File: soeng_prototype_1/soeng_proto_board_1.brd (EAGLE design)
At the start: 86.3 x 37.8 mm, 11 parts, among them J1 2172034-1

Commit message: PCB Rev. 2
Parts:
- removed CN1: (no value), adafruit:JST-PH-2-THM-RA
- added R1: 10, adafruit:0207/9
- added SPKR+, SPKR-: WIREPAD1,6/0,8, wirepad:1,6/0,8
- added T1: 2N2222, adafruit:TO92-EBC-OVAL
- moved C3 8.89 mm to (53.3, 30.5), turned to 180 degrees
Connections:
- new net N$9: R1.1, SPKR+.1
- net +5V: now also T1.C
- net GND: now also SPKR-.1
- net N$4: now also T1.B; no longer CN1.1
- net N$6: now also R1.2, T1.E; no longer CN1.2, U$1.1.5
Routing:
- net +5V: track 65.8 -> 81.1 mm
- net N$9: track 0.00 -> 10.8 mm
- net N$6: track 10.0 -> 6.11 mm
- net N$5: track 27.7 -> 30.9 mm
- net N$3: track 56.5 -> 59.6 mm, vias 0 -> 1
- net N$2: track 57.5 -> 55.9 mm
- net N$1: track 56.0 -> 57.1 mm
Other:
- board text added: "5V"
- board text added: "DIN"
- board text added: "Insert pushbuttons from other side, and match alignment of flats"
- board text added: "This end mates w/ TOP of 5-pin conn on right side of dot matrix displ"
- board text added: "VCC"
- board text removed: "+5V"

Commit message: Rev. 3
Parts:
- removed SPKR+, SPKR-: WIREPAD1,6/0,8, wirepad:1,6/0,8
- added U$4: MICRO_SPKR, lap_2019:MICRO_SPKR
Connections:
- net GND: now also U$4.P$2; no longer SPKR-.1
- net N$9: now also U$4.P$1; no longer SPKR+.1
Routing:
- net N$9: track 10.8 -> 9.49 mm
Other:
- board text added: "ALIGN FLATS IN PUSHBUTTONS WITH OUTLINE!!"
- board text added: "Engineering"
- board text added: "Insert pushbuttons from other side"
- board text added: "PN2222A"
- board text added: "SPKR+"
- board text added: "SPKR-"
- board text added: "TCNJ"
- board text removed: "Insert pushbuttons from other side, and match alignment of flats"
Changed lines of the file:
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@@
 <?xml version="1.0" encoding="utf-8"?>
 <!DOCTYPE eagle SYSTEM "eagle.dtd">
-<eagle version="9.5.2">
+<eagle version="9.6.2">
 <drawing>
 <settings>
@@
 <wire x1="29.718" y1="11.938" x2="29.718" y2="3.048" width="0.1524" layer="26" grouprefs="PUSHBUTTON1"/>
 <wire x1="29.718" y1="11.938" x2="29.718" y2="3.048" width="0.1524" layer="26" curve="-270" grouprefs="PUSHBUTTON1"/>
-<wire x1="11.43" y1="11.684" x2="11.43" y2="2.794" width="0.1524" layer="25" curve="-270"/>
-<wire x1="11.43" y1="11.684" x2="11.43" y2="2.794" width="0.1524" layer="25"/>
-<wire x1="29.464" y1="11.684" x2="29.464" y2="2.794" width="0.1524" layer="25"/>
-<wire x1="29.464" y1="11.684" x2="29.464" y2="2.794" width="0.1524" layer="25" curve="-270"/>
-<text x="19.05" y="11.43" size="1.016" layer="25">Insert pushbuttons from
-other side, and match
-alignment of flats</text>
+<text x="11.684" y="7.112" size="1.27" layer="25">Insert pushbuttons from other side</text>
+<text x="82.042" y="27.686" size="0.8128" layer="25">SPKR+</text>
+<text x="82.042" y="21.336" size="0.8128" layer="25">SPKR-</text>
+<text x="48.26" y="34.29" size="0.8128" layer="25">PN2222A</text>
+<text x="25.4" y="15.24" size="1.27" layer="26" rot="MR0" align="center">ALIGN FLATS IN PUSHBUTTONS
+WITH OUTLINE!!</text>
+<circle x="51.816" y="23.368" radius="0.254" width="0.1524" layer="22"/>
+<circle x="54.356" y="23.368" radius="0.254" width="0.1524" layer="22"/>
+<circle x="56.896" y="23.368" radius="0.254" width="0.1524" layer="22"/>
+<circle x="59.436" y="23.368" radius="0.254" width="0.1524" layer="22"/>
+<circle x="61.976" y="23.368" radius="0.254" width="0.1524" layer="22"/>
+<circle x="69.596" y="23.368" radius="0.254" width="0.1524" layer="22"/>
+<circle x="72.136" y="23.368" radius="0.254" width="0.1524" layer="22"/>
+<circle x="74.676" y="23.368" radius="0.254" width="0.1524" layer="22"/>
+<circle x="43.18" y="19.05" radius="0.254" width="0.1524" layer="22"/>
+<circle x="43.18" y="16.51" radius="0.254" width="0.1524" layer="22"/>
+<circle x="80.264" y="26.67" radius="0.254" width="0.1524" layer="22"/>
+<circle x="80.264" y="22.86" radius="0.254" width="0.1524" layer="22"/>
+<circle x="54.61" y="36.322" radius="0.254" width="0.1524" layer="22"/>
+<circle x="57.15" y="36.322" radius="0.254" width="0.1524" layer="22"/>
+<circle x="59.69" y="36.322" radius="0.254" width="0.1524" layer="22"/>
+<circle x="43.18" y="36.576" radius="0.254" width="0.1524" layer="22"/>
+<circle x="40.64" y="36.576" radius="0.254" width="0.1524" layer="22"/>
+<circle x="38.1" y="36.576" radius="0.254" width="0.1524" layer="22"/>
+<circle x="24.13" y="36.576" radius="0.254" width="0.1524" layer="22"/>
+<circle x="21.59" y="36.576" radius="0.254" width="0.1524" layer="22"/>
+<circle x="19.05" y="36.576" radius="0.254" width="0.1524" layer="22"/>
+<circle x="16.51" y="36.576" radius="0.254" width="0.1524" layer="22"/>
+<circle x="13.97" y="36.576" radius="0.254" width="0.1524" layer="22"/>
+<circle x="6.858" y="22.86" radius="0.254" width="0.1524" layer="22"/>
+<circle x="6.858" y="17.272" radius="0.254" width="0.1524" layer="22"/>
+<circle x="3.81" y="16.256" radius="0.254" width="0.1524" layer="22"/>
+<circle x="3.81" y="23.876" radius="0.254" width="0.1524" layer="22"/>
+<circle x="65.278" y="34.544" radius="0.254" width="0.1524" layer="21"/>
+<circle x="65.278" y="34.544" radius="0.254" width="0.1524" layer="22"/>
+<circle x="74.422" y="34.544" radius="0.254" width="0.1524" layer="22"/>
+<text x="63.5" y="17.78" size="6.4516" layer="22" rot="MR0" align="center">TCNJ</text>
+<text x="63.5" y="11.43" size="3.175" layer="22" rot="MR0" align="center">Engineering</text>
 </plain>
 <attributes>
@@
 <attribute name="VALUE" x="59.69" y="37.592" size="1.27" layer="27" ratio="10" rot="R180"/>
 </element>
-<element name="SPKR+" library="wirepad" library_urn="urn:adsk.eagle:library:412" package="1,6/0,8" package3d_urn="urn:adsk.eagle:package:30830/1" value="WIREPAD1,6/0,8" x="82.55" y="26.67" smashed="yes">
-<attribute name="NAME" x="79.248" y="27.686" size="1.27" layer="25" ratio="10"/>
-<attribute name="POPULARITY" value="1" x="82.55" y="26.67" size="1.778" layer="27" display="off"/>
-<attribute name="VALUE" x="82.55" y="27.27" size="0.0254" layer="27"/>
-</element>
-<element name="SPKR-" library="wirepad" library_urn="urn:adsk.eagle:library:412" package="1,6/0,8" package3d_urn="urn:adsk.eagle:package:30830/1" value="WIREPAD1,6/0,8" x="82.55" y="22.86" smashed="yes">
-<attribute name="NAME" x="79.248" y="23.876" size="1.27" layer="25" ratio="10"/>
-<attribute name="POPULARITY" value="1" x="82.55" y="22.86" size="1.778" layer="27" display="off"/>
-<attribute name="VALUE" x="82.55" y="23.46" size="0.0254" layer="27"/>
-</element>
 <element name="R1" library="adafruit" library_urn="urn:adsk.eagle:library:420" package="0207/9" package3d_urn="urn:adsk.eagle:package:6240935/1" value="10" x="69.85" y="33.02" smashed="yes" rot="R180">
 <attribute name="NAME" x="72.898" y="31.496" size="1.27" layer="25" ratio="10" rot="R180"/>
 <attribute name="VALUE" x="72.1106" y="33.655" size="1.27" layer="27" ratio="10" rot="R180"/>
 </element>
+<element name="U$4" library="lap_2019" package="MICRO_SPKR" value="MICRO_SPKR" x="81.28" y="26.67" smashed="yes" rot="R270"/>
 </elements>
 <signals>
@@
 <contactref element="C1" pad="2"/>
 <contactref element="DOT_MATRIX_DISPLAY" pad="2"/>
-<contactref element="SPKR-" pad="1"/>
+<contactref element="U$4" pad="P$2"/>
 </signal>
 <signal name="+5V">
@@
 <signal name="N$9">
 <contactref element="R1" pad="1"/>
-<contactref element="SPKR+" pad="1"/>
-<wire x1="80.772" y1="26.67" x2="82.55" y2="26.67" width="0.1524" layer="1"/>
+<contactref element="U$4" pad="P$1"/>
+<wire x1="80.772" y1="26.67" x2="81.28" y2="26.67" width="0.1524" layer="1"/>
 <wire x1="74.422" y1="33.02" x2="80.772" y2="26.67" width="0.1524" layer="1"/>
 </signal>

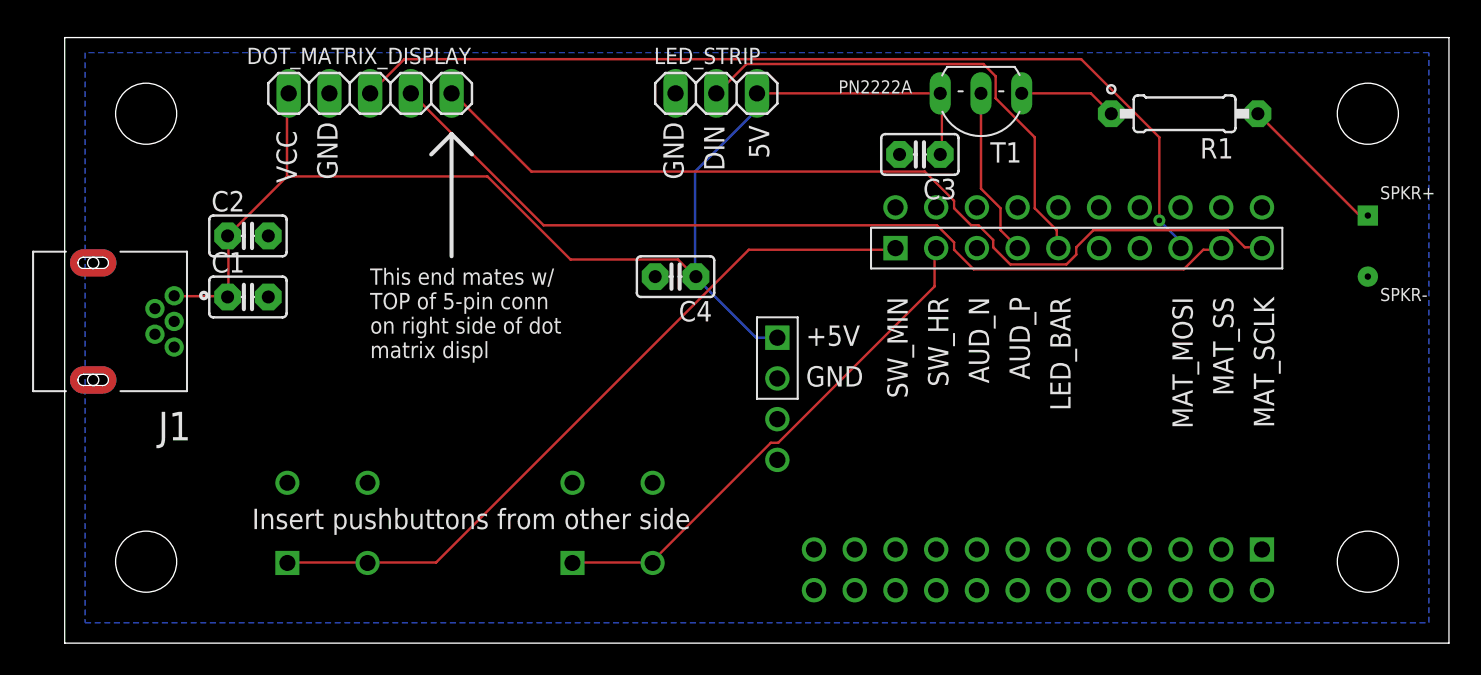
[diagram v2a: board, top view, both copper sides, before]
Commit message: Added TCXO, 3.3V Zener, RC
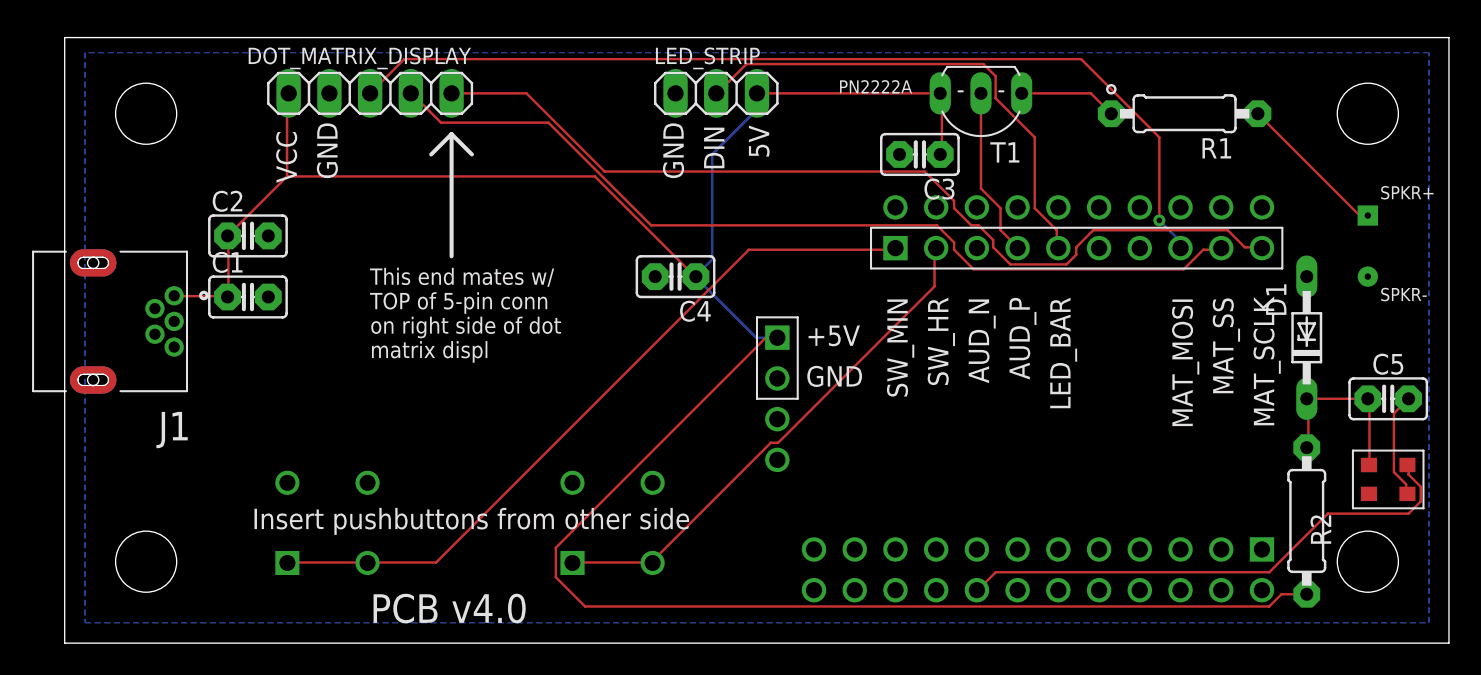
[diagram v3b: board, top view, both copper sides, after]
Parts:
- added C5: (no value), adafruit:C025-025X050
- added D1: (no value), diode:DO34Z7
- added R2: 10, adafruit:0207/9
- added U$5: TXEAPLSANF, lap_2019:TXEAPLSANF
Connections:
- new net N$10: U$1.2.7, U$5.TCXO3
- new net N$11: C5.1, D1.C, R2.1, U$5.TCXO4
- net +5V: now also R2.2
- net GND: now also C5.2, D1.A, U$5.TCXO2
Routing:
- net +5V: track 81.1 -> 150.1 mm
- net N$10: track 0.00 -> 32.6 mm
- net N$11: track 0.00 -> 11.2 mm
- net GND: track 0.00 -> 6.65 mm
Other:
- board text added: "Larry Pearlstein, Elli Lopez"
- board text added: "PCB v4.0"
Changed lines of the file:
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@@
 <text x="63.5" y="17.78" size="6.4516" layer="22" rot="MR0" align="center">TCNJ</text>
 <text x="63.5" y="11.43" size="3.175" layer="22" rot="MR0" align="center">Engineering</text>
+<text x="74.93" y="7.62" size="0.762" layer="22" rot="MR0">Larry Pearlstein, Elli Lopez</text>
+<text x="19.05" y="1.27" size="1.778" layer="25">PCB v4.0</text>
 </plain>
 <attributes>
@@
 </element>
 <element name="U$4" library="lap_2019" package="MICRO_SPKR" value="MICRO_SPKR" x="81.28" y="26.67" smashed="yes" rot="R270"/>
+<element name="U$5" library="lap_2019" package="TXEAPLSANF" value="TXEAPLSANF" x="82.55" y="10.16" smashed="yes"/>
+<element name="D1" library="diode" library_urn="urn:adsk.eagle:library:210" package="DO34Z7" package3d_urn="urn:adsk.eagle:package:43364/1" value="" x="77.47" y="19.05" smashed="yes" rot="R90">
+<attribute name="NAME" x="76.2" y="20.32" size="1.27" layer="25" ratio="10" rot="R90"/>
+<attribute name="POPULARITY" value="3" x="77.47" y="19.05" size="1.778" layer="27" rot="R90" display="off"/>
+<attribute name="VALUE" x="79.883" y="17.526" size="1.27" layer="27" ratio="10" rot="R90"/>
+</element>
+<element name="R2" library="adafruit" library_urn="urn:adsk.eagle:library:420" package="0207/9" package3d_urn="urn:adsk.eagle:package:6240935/1" value="10" x="77.47" y="7.62" smashed="yes" rot="R270">
+<attribute name="NAME" x="77.724" y="8.128" size="1.27" layer="25" ratio="10" rot="R270"/>
+<attribute name="VALUE" x="76.835" y="9.8806" size="1.27" layer="27" ratio="10" rot="R270"/>
+</element>
+<element name="C5" library="adafruit" library_urn="urn:adsk.eagle:library:420" package="C025-025X050" package3d_urn="urn:adsk.eagle:package:6240323/1" value="" x="82.55" y="15.24" smashed="yes">
+<attribute name="NAME" x="81.534" y="16.764" size="1.27" layer="25" ratio="10"/>
+<attribute name="VALUE" x="80.264" y="12.446" size="1.27" layer="27" ratio="10"/>
+</element>
 </elements>
 <signals>
@@
 <wire x1="55.4736" y1="27.5844" x2="55.4736" y2="27.1272" width="0.1524" layer="1"/>
 <wire x1="53.6448" y1="29.4132" x2="55.4736" y2="27.5844" width="0.1524" layer="1"/>
-<wire x1="29.1084" y1="29.4132" x2="53.6448" y2="29.4132" width="0.1524" layer="1"/>
-<wire x1="24.2316" y1="34.29" x2="29.1084" y2="29.4132" width="0.1524" layer="1"/>
+<wire x1="33.6804" y1="29.4132" x2="53.6448" y2="29.4132" width="0.1524" layer="1"/>
+<wire x1="28.8036" y1="34.29" x2="33.6804" y2="29.4132" width="0.1524" layer="1"/>
+<wire x1="24.13" y1="34.29" x2="28.8036" y2="34.29" width="0.1524" layer="1"/>
 <wire x1="74.676" y1="24.6888" x2="74.676" y2="24.638" width="0.1524" layer="1"/>
-<wire x1="24.2316" y1="34.29" x2="24.13" y2="34.29" width="0.1524" layer="1"/>
 </signal>
 <signal name="N$2">
@@
 <wire x1="55.4736" y1="24.9936" x2="55.4736" y2="24.5364" width="0.1524" layer="1"/>
 <wire x1="54.4068" y1="26.0604" x2="55.4736" y2="24.9936" width="0.1524" layer="1"/>
-<wire x1="29.8704" y1="26.0604" x2="54.4068" y2="26.0604" width="0.1524" layer="1"/>
-<wire x1="21.6408" y1="34.29" x2="29.8704" y2="26.0604" width="0.1524" layer="1"/>
+<wire x1="36.576" y1="26.0604" x2="54.4068" y2="26.0604" width="0.1524" layer="1"/>
+<wire x1="30.1752" y1="32.4612" x2="36.576" y2="26.0604" width="0.1524" layer="1"/>
+<wire x1="23.4696" y1="32.4612" x2="30.1752" y2="32.4612" width="0.1524" layer="1"/>
+<wire x1="21.6408" y1="34.29" x2="23.4696" y2="32.4612" width="0.1524" layer="1"/>
 <wire x1="72.0852" y1="24.5364" x2="72.136" y2="24.638" width="0.1524" layer="1"/>
 <wire x1="21.6408" y1="34.29" x2="21.59" y2="34.29" width="0.1524" layer="1"/>
@@
 <contactref element="DOT_MATRIX_DISPLAY" pad="2"/>
 <contactref element="U$4" pad="P$2"/>
+<contactref element="U$5" pad="TCXO2"/>
+<contactref element="D1" pad="A"/>
+<contactref element="C5" pad="2"/>
+<wire x1="83.6676" y1="9.906" x2="83.6676" y2="9.4488" width="0.1524" layer="1"/>
+<wire x1="82.9056" y1="10.668" x2="83.6676" y2="9.906" width="0.1524" layer="1"/>
+<wire x1="82.9056" y1="14.3256" x2="82.9056" y2="10.668" width="0.1524" layer="1"/>
+<wire x1="83.82" y1="15.24" x2="82.9056" y2="14.3256" width="0.1524" layer="1"/>
+<wire x1="83.6676" y1="9.4488" x2="83.75" y2="9.31" width="0.1524" layer="1"/>
 </signal>
 <signal name="+5V">
@@
 <contactref element="DOT_MATRIX_DISPLAY" pad="1"/>
 <contactref element="T1" pad="C"/>
+<contactref element="R2" pad="2"/>
 <wire x1="10.0584" y1="21.6408" x2="6.858" y2="21.6408" width="0.1524" layer="1"/>
 <wire x1="6.858" y1="21.6408" x2="6.828" y2="21.666" width="0.1524" layer="1"/>
@@
 <wire x1="10.2108" y1="21.6408" x2="10.16" y2="21.59" width="0.1524" layer="1"/>
 <wire x1="10.2108" y1="25.2984" x2="10.16" y2="25.4" width="0.1524" layer="1"/>
-<wire x1="43.1292" y1="19.05" x2="44.45" y2="19.05" width="0.1524" layer="16"/>
-<wire x1="39.3192" y1="22.86" x2="43.1292" y2="19.05" width="0.1524" layer="16"/>
 <wire x1="54.7116" y1="30.48" x2="54.7116" y2="34.29" width="0.1524" layer="1"/>
 <wire x1="54.7116" y1="34.29" x2="54.61" y2="34.29" width="0.1524" layer="1"/>
 <wire x1="54.7116" y1="30.48" x2="54.61" y2="30.48" width="0.1524" layer="1"/>
 <wire x1="54.61" y1="34.29" x2="43.18" y2="34.29" width="0.1524" layer="1"/>
-<wire x1="39.3192" y1="29.4132" x2="39.3192" y2="22.86" width="0.1524" layer="16"/>
-<wire x1="43.1292" y1="33.2232" x2="39.3192" y2="29.4132" width="0.1524" layer="16"/>
-<wire x1="43.1292" y1="34.29" x2="43.1292" y2="33.2232" width="0.1524" layer="16"/>
+<wire x1="43.1292" y1="19.05" x2="44.45" y2="19.05" width="0.1524" layer="16"/>
+<wire x1="39.3192" y1="22.86" x2="43.1292" y2="19.05" width="0.1524" layer="16"/>
+<wire x1="75.8952" y1="3.048" x2="77.47" y2="3.048" width="0.1524" layer="1"/>
+<wire x1="75.1332" y1="2.286" x2="75.8952" y2="3.048" width="0.1524" layer="1"/>
+<wire x1="32.4612" y1="2.286" x2="75.1332" y2="2.286" width="0.1524" layer="1"/>
+<wire x1="30.6324" y1="4.1148" x2="32.4612" y2="2.286" width="0.1524" layer="1"/>
+<wire x1="30.6324" y1="5.9436" x2="30.6324" y2="4.1148" width="0.1524" layer="1"/>
+<wire x1="43.7388" y1="19.05" x2="30.6324" y2="5.9436" width="0.1524" layer="1"/>
+<wire x1="44.45" y1="19.05" x2="43.7388" y2="19.05" width="0.1524" layer="1"/>
+<wire x1="43.1292" y1="33.2232" x2="43.1292" y2="34.29" width="0.1524" layer="16"/>
+<wire x1="40.386" y1="30.48" x2="43.1292" y2="33.2232" width="0.1524" layer="16"/>
+<wire x1="40.386" y1="23.9268" x2="40.386" y2="30.48" width="0.1524" layer="16"/>
+<wire x1="39.3192" y1="22.86" x2="40.386" y2="23.9268" width="0.1524" layer="16"/>
+<wire x1="43.1292" y1="34.29" x2="43.18" y2="34.29" width="0.1524" layer="16"/>
 <wire x1="39.3192" y1="22.86" x2="39.37" y2="22.86" width="0.1524" layer="16"/>
-<wire x1="43.1292" y1="34.29" x2="43.18" y2="34.29" width="0.1524" layer="16"/>
-<wire x1="26.3652" y1="29.1084" x2="13.8684" y2="29.1084" width="0.1524" layer="1"/>
-<wire x1="31.5468" y1="23.9268" x2="26.3652" y2="29.1084" width="0.1524" layer="1"/>
-<wire x1="38.2524" y1="23.9268" x2="31.5468" y2="23.9268" width="0.1524" layer="1"/>
-<wire x1="39.3192" y1="22.86" x2="38.2524" y2="23.9268" width="0.1524" layer="1"/>
+<wire x1="33.0708" y1="29.1084" x2="13.8684" y2="29.1084" width="0.1524" layer="1"/>
+<wire x1="39.3192" y1="22.86" x2="33.0708" y2="29.1084" width="0.1524" layer="1"/>
 <wire x1="39.3192" y1="22.86" x2="39.37" y2="22.86" width="0.1524" layer="1"/>
 </signal>
@@
 <wire x1="74.422" y1="33.02" x2="80.772" y2="26.67" width="0.1524" layer="1"/>
 </signal>
+<signal name="N$10">
+<contactref element="U$5" pad="TCXO3"/>
+<contactref element="U$1" pad="2.7"/>
+<wire x1="83.82" y1="10.5156" x2="83.82" y2="10.9728" width="0.1524" layer="1"/>
+<wire x1="84.582" y1="9.7536" x2="83.82" y2="10.5156" width="0.1524" layer="1"/>
+<wire x1="84.582" y1="8.8392" x2="84.582" y2="9.7536" width="0.1524" layer="1"/>
+<wire x1="83.82" y1="8.0772" x2="84.582" y2="8.8392" width="0.1524" layer="1"/>
+<wire x1="78.7908" y1="8.0772" x2="83.82" y2="8.0772" width="0.1524" layer="1"/>
+<wire x1="75.1332" y1="4.4196" x2="78.7908" y2="8.0772" width="0.1524" layer="1"/>
+<wire x1="58.0644" y1="4.4196" x2="75.1332" y2="4.4196" width="0.1524" layer="1"/>
+<wire x1="56.9976" y1="3.3528" x2="58.0644" y2="4.4196" width="0.1524" layer="1"/>
+<wire x1="83.82" y1="10.9728" x2="83.75" y2="11.11" width="0.1524" layer="1"/>
+<wire x1="56.9976" y1="3.3528" x2="56.896" y2="3.302" width="0.1524" layer="1"/>
+</signal>
+<signal name="N$11">
+<contactref element="R2" pad="1"/>
+<contactref element="D1" pad="C"/>
+<contactref element="C5" pad="1"/>
+<contactref element="U$5" pad="TCXO4"/>
+<wire x1="81.3816" y1="15.24" x2="81.3816" y2="11.1252" width="0.1524" layer="1"/>
+<wire x1="81.3816" y1="11.1252" x2="81.35" y2="11.11" width="0.1524" layer="1"/>
+<wire x1="81.3816" y1="15.24" x2="81.28" y2="15.24" width="0.1524" layer="1"/>
+<wire x1="77.5716" y1="12.192" x2="77.5716" y2="15.24" width="0.1524" layer="1"/>
+<wire x1="77.5716" y1="12.192" x2="77.47" y2="12.192" width="0.1524" layer="1"/>
+<wire x1="77.5716" y1="15.24" x2="81.28" y2="15.24" width="0.1524" layer="1"/>
+<wire x1="77.5716" y1="15.24" x2="77.47" y2="15.24" width="0.1524" layer="1"/>
+</signal>
 </signals>
